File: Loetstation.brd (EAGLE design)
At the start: 52.1 x 47 mm, 68 parts, among them IC1 ATMEGA328PB-AU, IC2 LM75AD,112, IC3 CD4050BD, IC4 7805DT, IC5 AMS1117-3.3V, IC6 TL082D, J1 22-27-2021-02, J2 AVR_SPI_PROG_3X2TESTPOINTS, J3 22-27-2041-04, J4 22-27-2041-04, T1 SI7489DP-T1-E3, T2 SI7489DP-T1-E3, T3 BC847, T4 BC847, X1 CSTCE16M0V53-R0, X3 DISPLAY_TFT_1,8, X4 22-27-2051-05

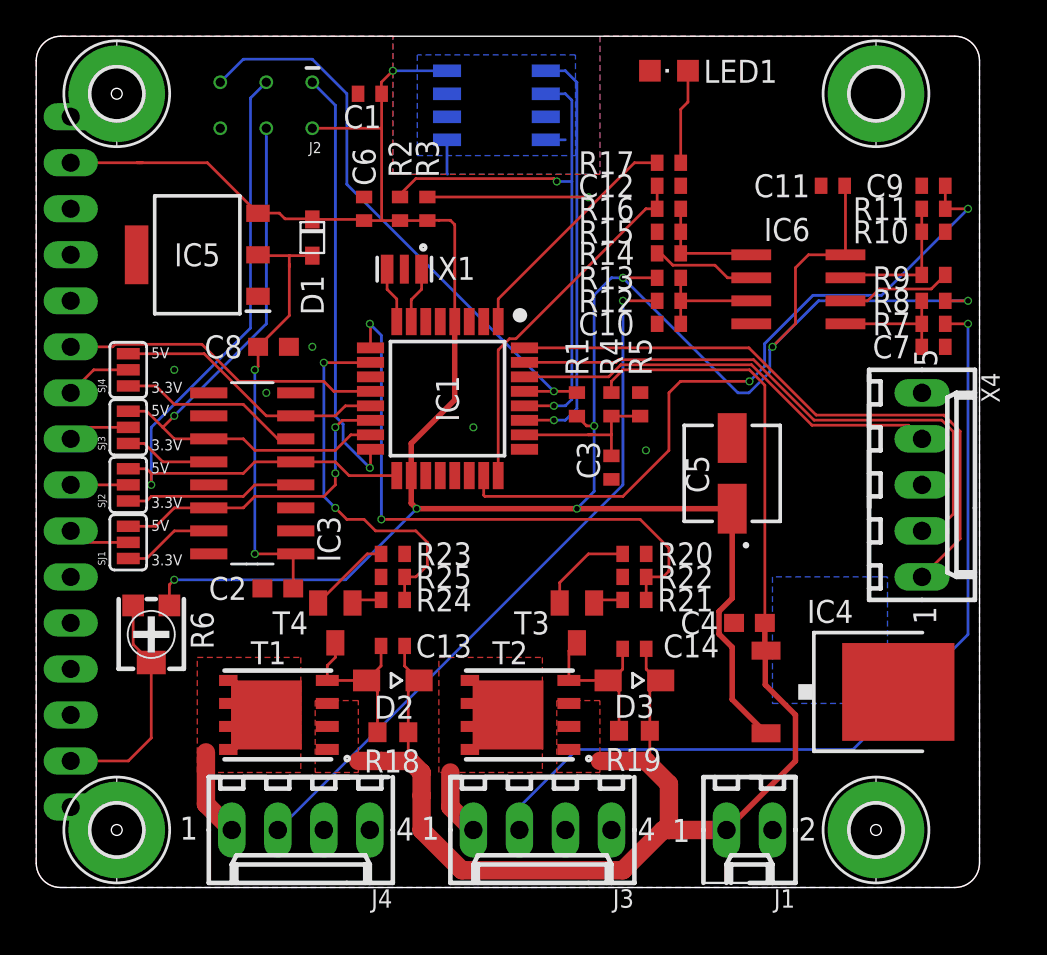
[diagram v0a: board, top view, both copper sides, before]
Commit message: Power-MOSFETs durch FDS9435A getauscht
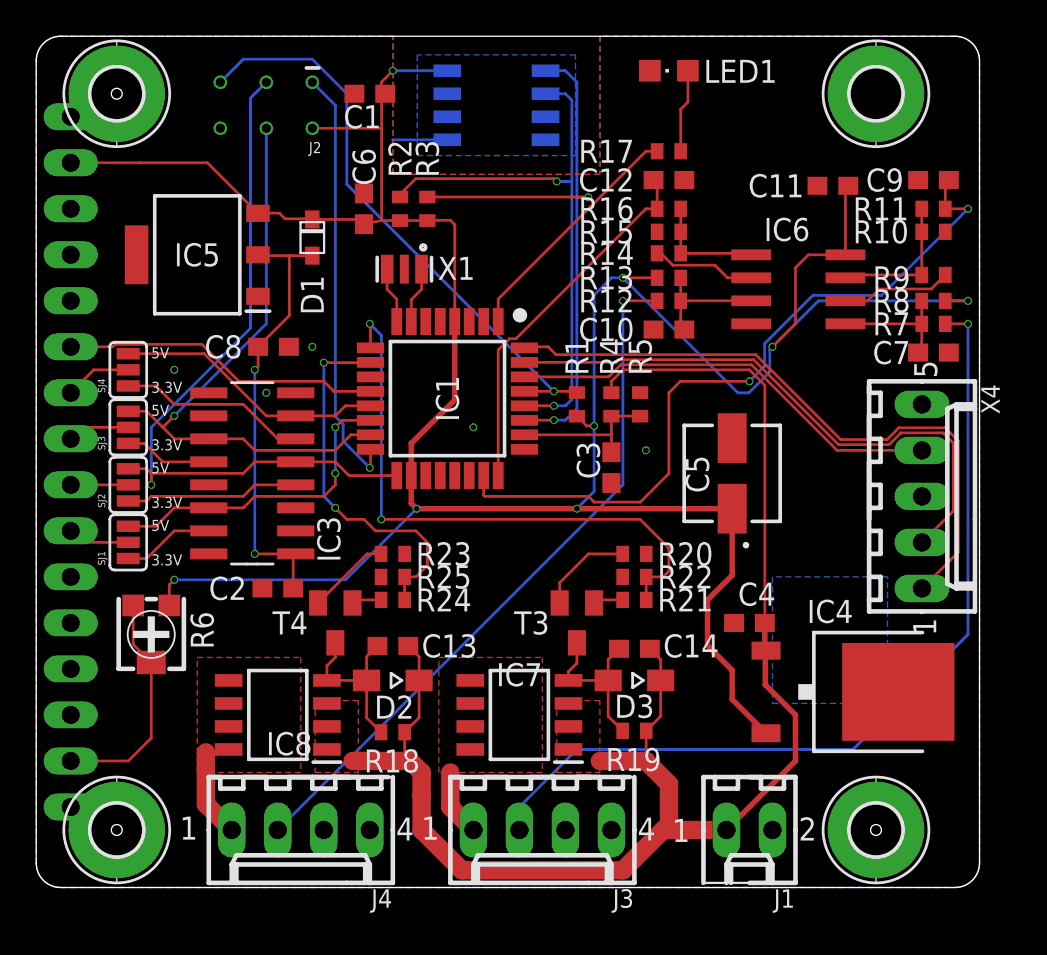
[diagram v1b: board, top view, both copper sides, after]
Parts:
- removed T1, T2: SI7489DP-T1-E3, SamacSys_Parts:POWERPAKSO-8
- added IC7, IC8: FDS9435A, SamacSys_Parts:SOIC127P600X175-8N
- C1, C10, C11, C12, C13, C14, C3, C6, C7, C9: device resistor:C0402 -> resistor:C0603
- D1: value (none) -> 1N4148WS
- R18, R19: device resistor:R0603 -> resistor:R0402
- moved X4 0.64 mm to (48.9, 21.6)
- moved R17 0.63 mm to (34.9, 40.6)
- moved C12 0.32 mm to (34.9, 39.1)
- moved C9 0.32 mm to (49.5, 39.1)
- moved C10 0.32 mm to (34.9, 30.8)
- moved C7 0.32 mm to (49.5, 29.5)
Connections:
- net KOLBEN1: now also IC7.5, IC7.6, IC7.7, IC7.8; no longer T2.5, T2.6, T2.7, T2.8, T2.9
- net KOLBEN2: now also IC8.5, IC8.6, IC8.7, IC8.8; no longer T1.5, T1.6, T1.7, T1.8, T1.9
- net N$4: now also IC8.4; no longer T1.4
- net N$5: now also IC7.4; no longer T2.4
- net V_IN: now also IC7.1, IC7.2, IC7.3, IC8.1, IC8.2, IC8.3; no longer T1.1, T1.2, T1.3, T2.1, T2.2, T2.3
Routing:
- net ANALOG_KOLBEN1: track 39.5 -> 40.9 mm
- net N$21: track 34.9 -> 35.6 mm
- net N$20: track 5.25 -> 4.61 mm
- net V_IN: track 83.7 -> 83.2 mm

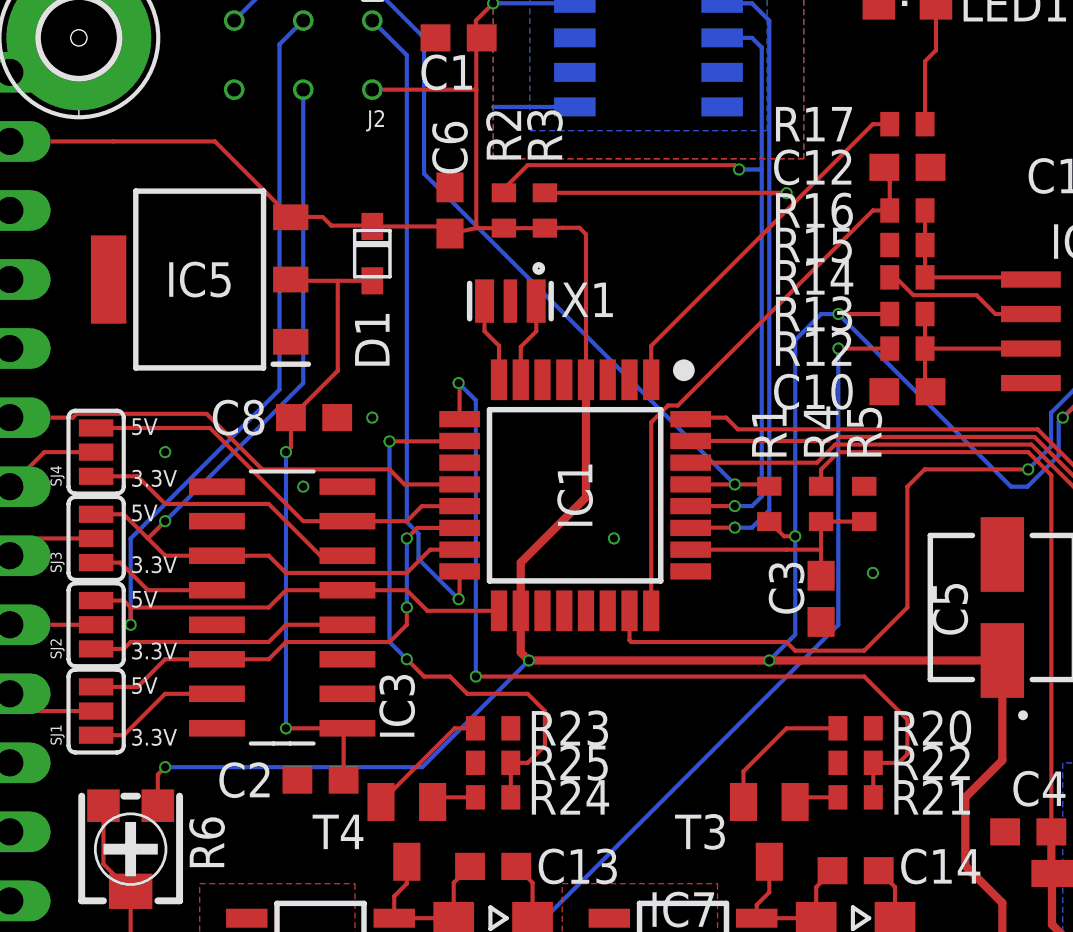
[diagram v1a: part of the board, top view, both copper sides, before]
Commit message: Abblock Kondensatoren für µC hinzugefügt
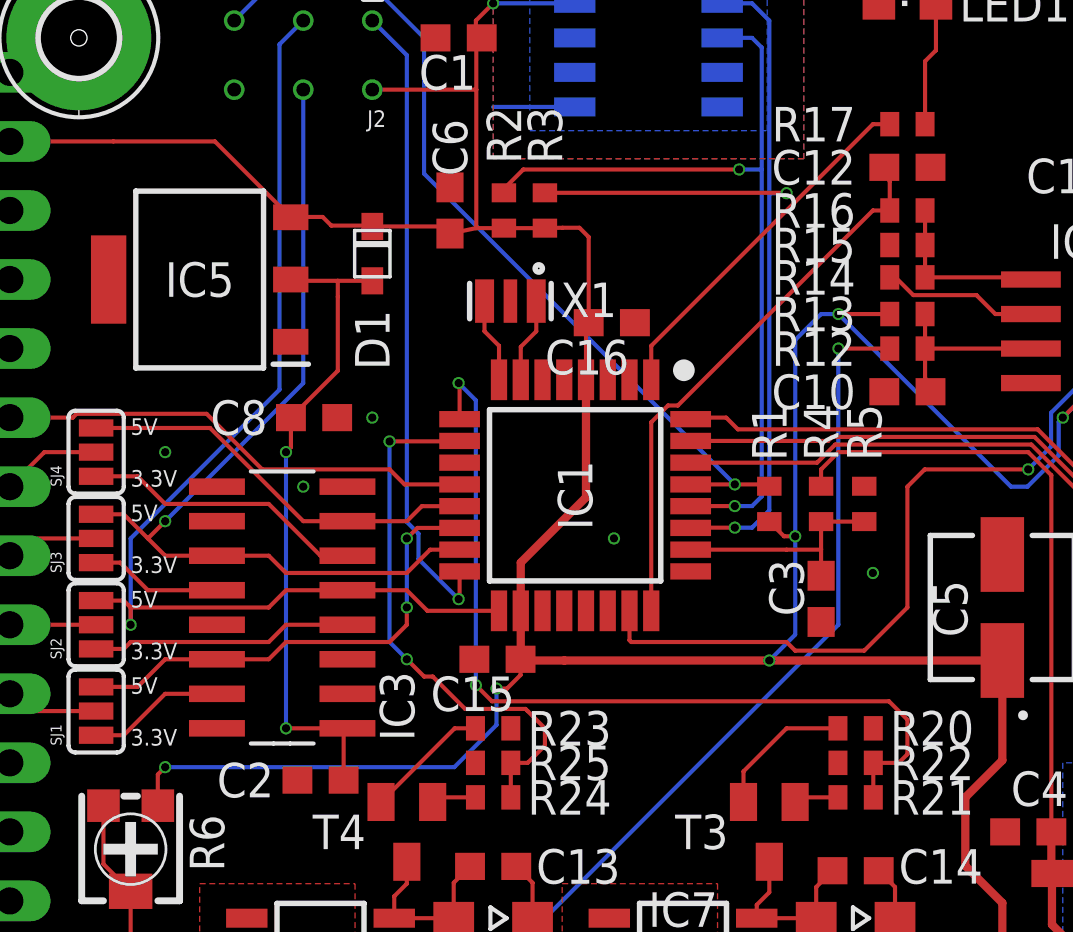
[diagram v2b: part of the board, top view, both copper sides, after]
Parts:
- added C15, C16: 100n, resistor:C0603
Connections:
- net GND: now also C15.2, C16.1
- net VCC: now also C15.1, C16.2
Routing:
- net VCC: track 158.3 -> 159.5 mm
